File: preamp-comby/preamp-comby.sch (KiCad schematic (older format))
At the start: 20 parts

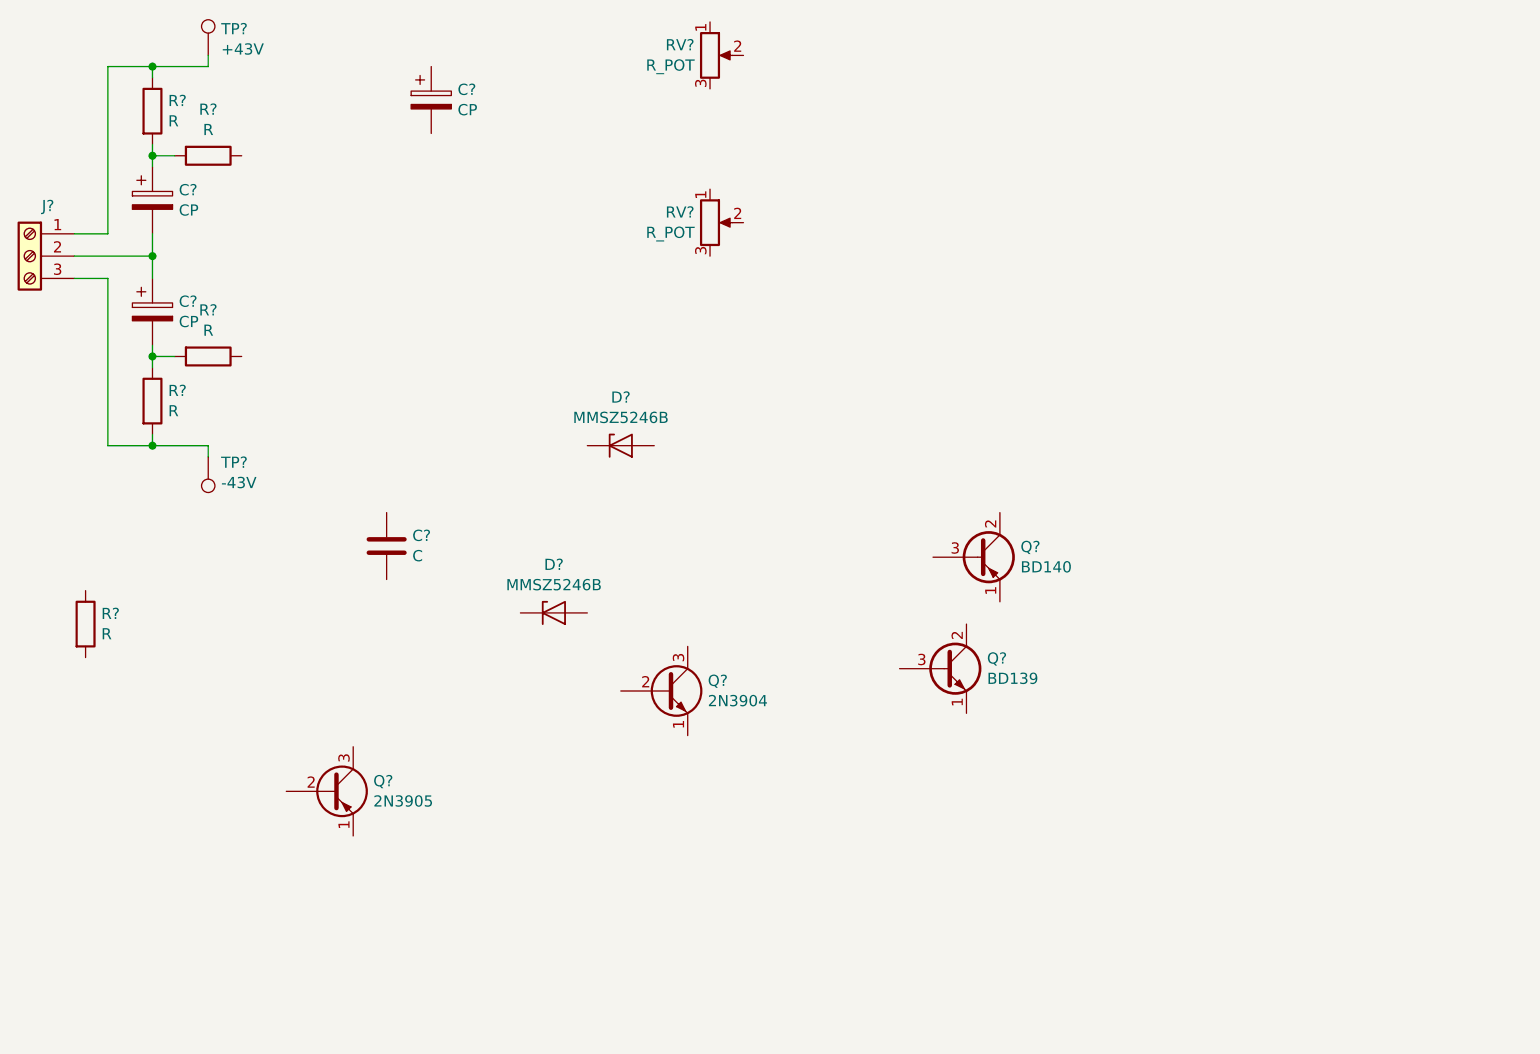
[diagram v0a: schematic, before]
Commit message: Draw schematic of comby
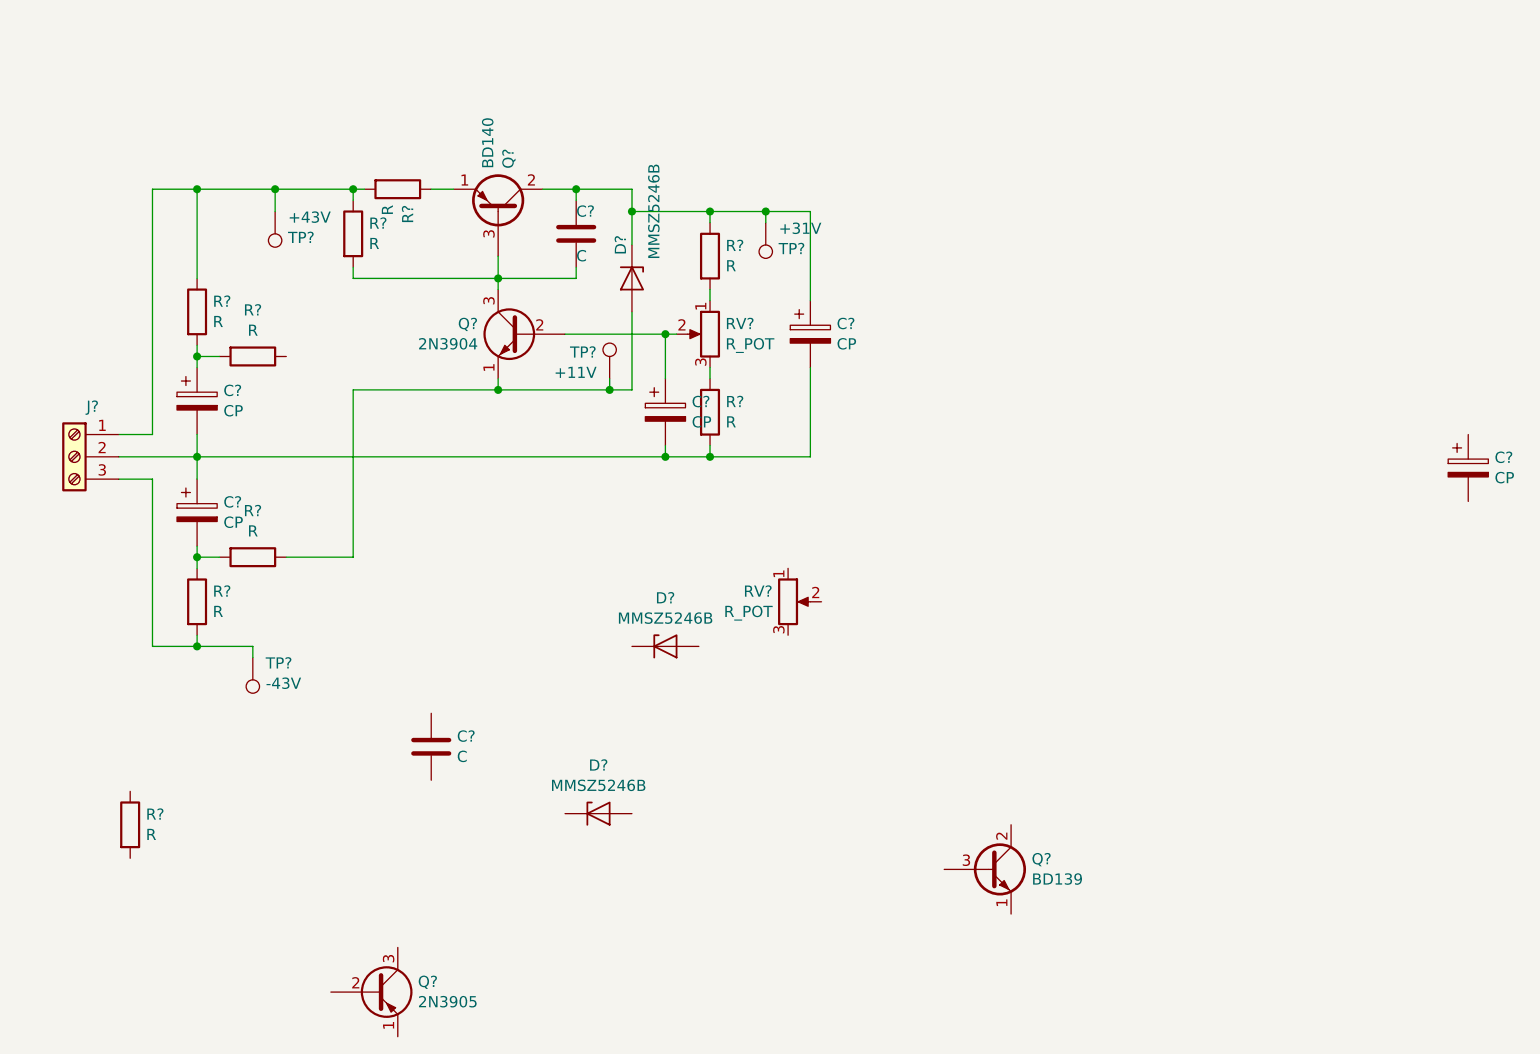
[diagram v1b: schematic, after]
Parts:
- added C?: C, symbol Device:C
- added C? (x2): CP, symbol Device:CP
- added D?: MMSZ5246B, Diode_SMD:D_SOD-123, symbol Diode:BZT52Bxx
- added R? (x4): R, symbol Device:R
- added TP?: +11V, symbol Connector:TestPoint
- added TP?: +31V, symbol Connector:TestPoint
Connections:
- net at Q?.1 (E): now also R?.1
- net at Q?.2 (C): now also C?.1, C?.1, D?.1 (K), R?.1, TP?.1
- net at Q?.3 (B): now also Q?.3 (C), C?.2, R?.2
- net at Q?.1 (E): now also R?.1, D?.2 (A), TP?.1
- net at Q?.2 (B): now also RV?.2, C?.1
- net at RV?.1: now also R?.2
- net at RV?.3: now also R?.1
- net at J?.1 (Pin_1), R?.1, TP?.1: now also R?.1, R?.2
- net at C?.1, C?.2, J?.2 (Pin_2): now also C?.2, C?.2, R?.2
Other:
- moved on the sheet: C?, D?, J?, Q?, R?, RV?, TP?
